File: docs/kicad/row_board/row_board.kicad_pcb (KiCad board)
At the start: 2 copper layers, 200 x 25 mm, 19 parts, among them J1 Conn_01x06, J2 Conn_01x06, SW1 SW1, SW2 SW1, SW3 SW1, SW4 SW1, SW5 SW1, U1 74HC595

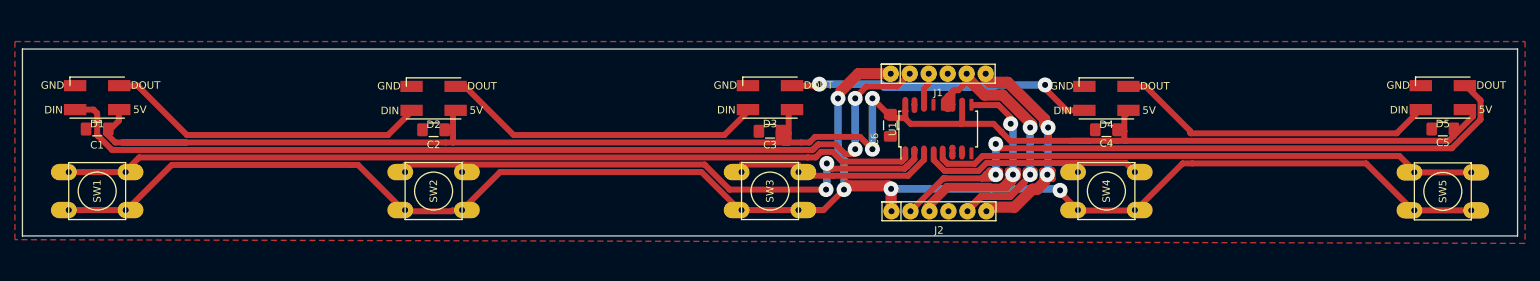
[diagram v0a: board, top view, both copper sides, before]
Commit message: new row board design (with chip at left end)
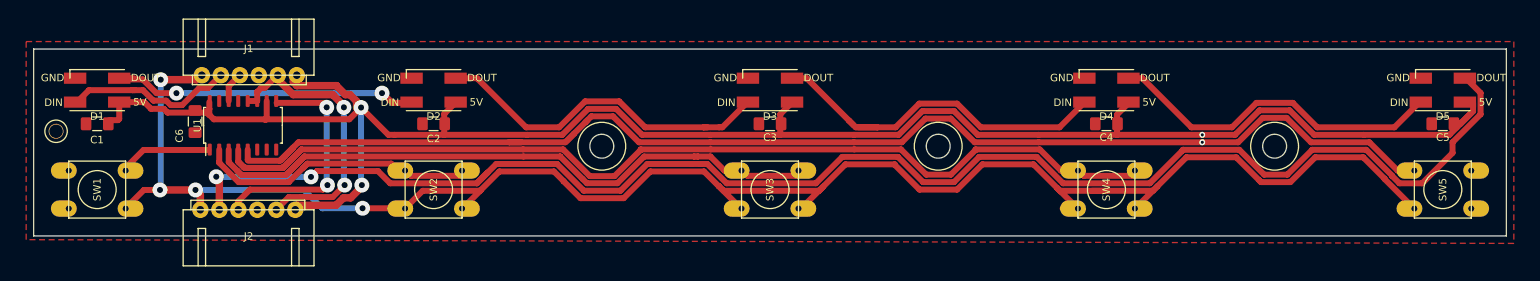
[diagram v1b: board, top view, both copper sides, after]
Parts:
- added REF**: myMountingHole_1.8mm, 0_my_footprints:myMountingHole_1.8mm, F.Cu at (54.5, 86.0)
- added REF**: myMountingHole_3.2mm_M3, 0_my_footprints:myMountingHole_3.2mm_M3, F.Cu at (217.5, 88.0)
- added REF**: myMountingHole_3.2mm_M3, 0_my_footprints:myMountingHole_3.2mm_M3, F.Cu at (172.5, 88.0)
- added REF**: myMountingHole_3.2mm_M3, 0_my_footprints:myMountingHole_3.2mm_M3, F.Cu at (127.5, 88.0)
- J1, J2: footprint 0_my_footprints:my6Pin-08mm -> 0_my_footprints:invRightAngleJSTx06
- moved J1 98.5 mm to (74.0, 78.5)
- moved C6 93.0 mm to (73.1, 84.7)
- moved U1 93.0 mm to (79.5, 85.2)
- moved J2 86.1 mm to (86.5, 96.5), turned to 180 degrees
- moved D2 1.10 mm to (105.0, 80.5)
- moved D4 1.10 mm to (195.0, 80.5)
- moved C3 1.00 mm to (150.0, 85.0)
- moved D1 1.00 mm to (60.0, 80.5)
- moved D3 1.00 mm to (150.0, 80.5)
- moved D5 1.00 mm to (240.0, 80.5)
- moved C2 0.80 mm to (105.0, 85.0)
- moved C4 0.80 mm to (195.0, 85.0)
- moved C1 0.70 mm to (60.0, 85.0)
- moved C5 0.70 mm to (240.0, 85.0)
- moved SW5 0.24 mm to (240.0, 93.8)
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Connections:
- J2 pad 1: BTN_SENSE -> +5V
- J2 pad 2: LED_DOUT -> BTN_CLK
- J2 pad 3: BTN_DOUT -> GND
- J2 pad 4: GND -> BTN_DOUT
- J2 pad 5: BTN_CLK -> LED_DOUT
- J2 pad 6: +5V -> BTN_SENSE
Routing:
- net Net-(SW4-Pad1): track 31.2 -> 142.3 mm
- net LED_DOUT: track 96.4 -> 204.8 mm
- net LED_DIN: track 126.1 -> 22.6 mm, vias 2 -> 0
- net Net-(SW1-Pad1): track 114.9 -> 12.4 mm
- net Net-(SW5-Pad1): track 73.7 -> 174.0 mm, vias 0 -> 1
- net Net-(SW3-Pad1): track 30.1 -> 87.9 mm
- net Net-(SW2-Pad1): track 79.5 -> 38.0 mm, vias 2 -> 0
- net +5V: track 273.3 -> 255.3 mm, vias 4 -> 3
- net BTN_DOUT: track 46.8 -> 31.9 mm
- net BTN_SENSE: track 230.1 -> 244.9 mm
- net Net-(D3-Pad2): track 40.3 -> 49.4 mm, vias 2 -> 0
- net BTN_CLK: track 43.7 -> 37.8 mm
- net Net-(D2-Pad2): track 43.3 -> 46.5 mm
- net Net-(D1-Pad2): track 43.4 -> 41.0 mm, vias 0 -> 2
- net Net-(D4-Pad2): track 43.5 -> 45.8 mm
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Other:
- board size 200 x 25 mm -> 197 x 25 mm
- board text removed: "NEEDS: Mounting Holes Ground Crossings -1 mm in height/width"

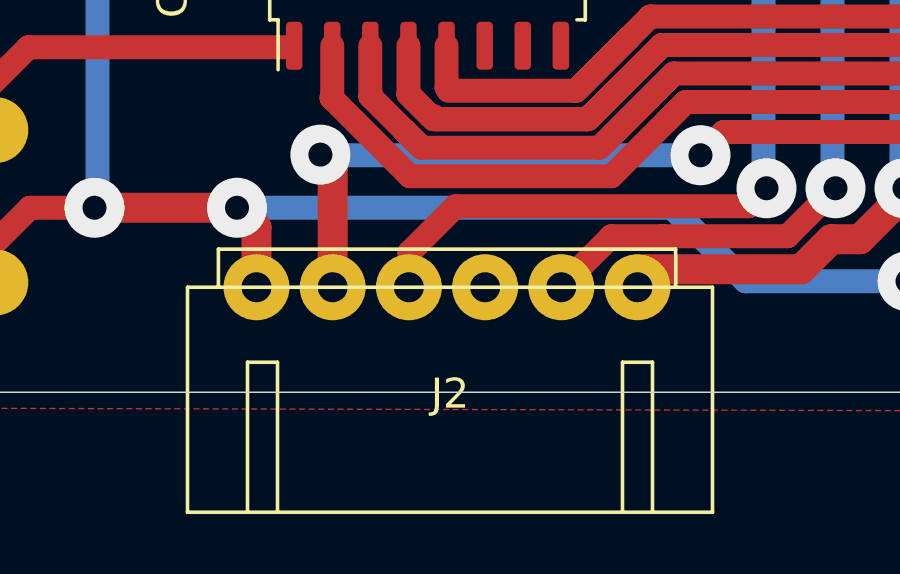
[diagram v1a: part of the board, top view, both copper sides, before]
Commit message: kicad changes to support actual Fusion 360 TE3 design efforts - created rotary board PCB
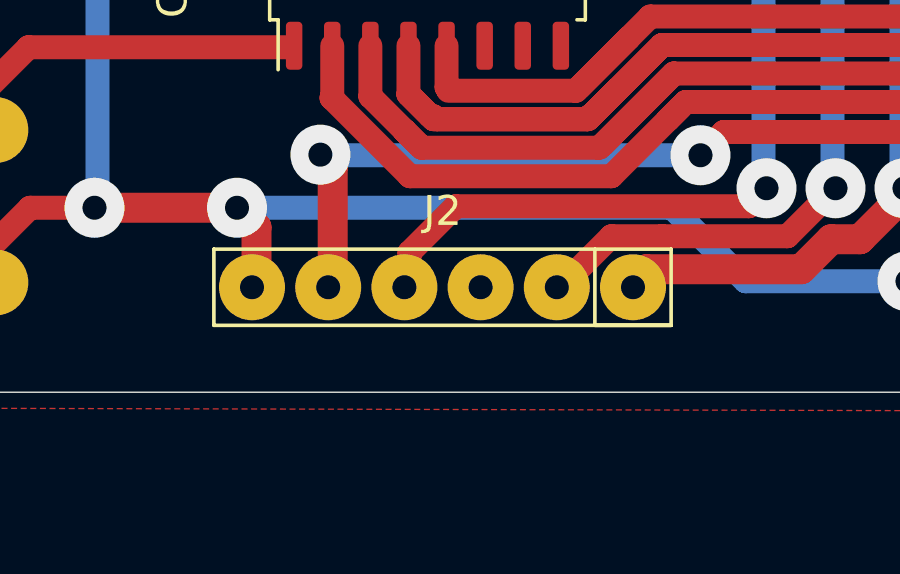
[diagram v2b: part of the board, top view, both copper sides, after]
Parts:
- J2: footprint 0_my_footprints:invRightAngleJSTx06 -> 0_my_footprints:my6Pin-08mm
- moved J2 6.50 mm to (80.0, 96.5)

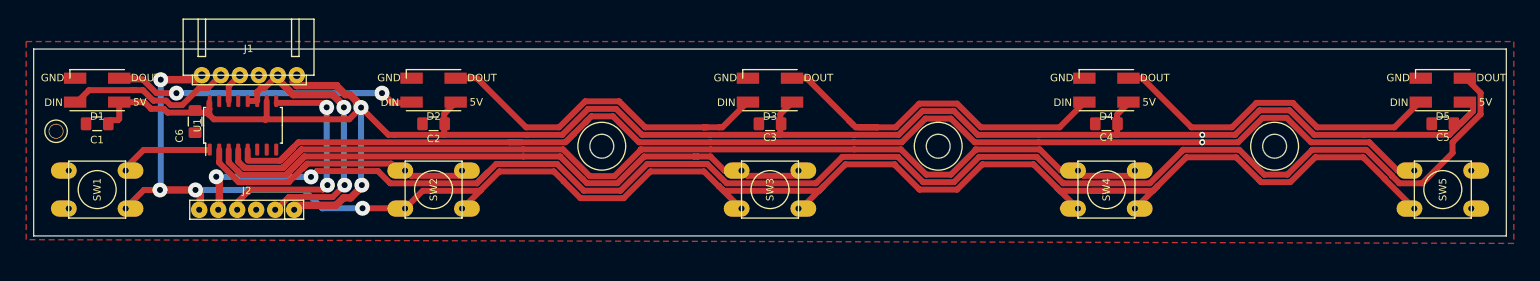
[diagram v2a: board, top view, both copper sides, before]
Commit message: cutting actual TE3 milled circuit boards
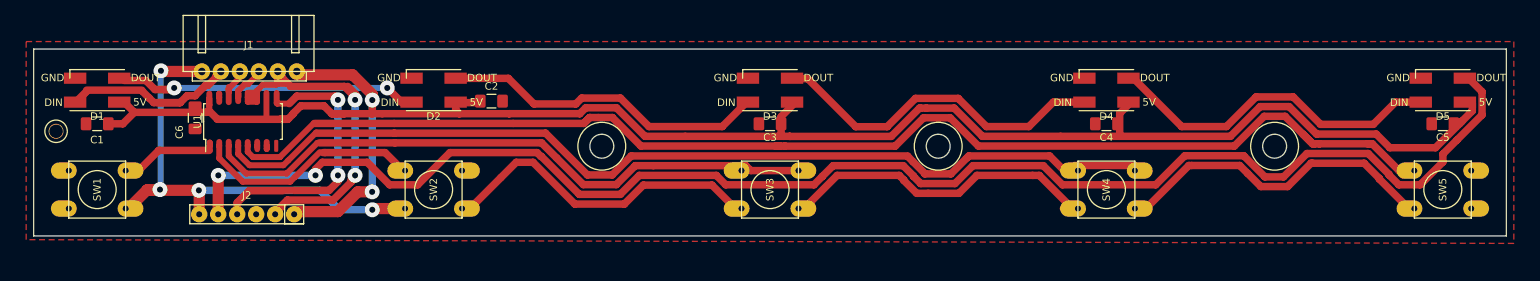
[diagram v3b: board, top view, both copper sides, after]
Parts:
- moved C2 8.31 mm to (112.7, 82.0), turned to 0 degrees
- moved J2 0.60 mm to (80.0, 97.1)
- moved C6 0.50 mm to (73.1, 84.2)
- moved J1 0.50 mm to (74.0, 78.0)
- moved U1 0.50 mm to (79.5, 84.7)
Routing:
- net BTN_SENSE: track 244.9 -> 202.1 mm
- net BTN_DOUT: track 31.9 -> 51.2 mm
- net BTN_CLK: track 37.8 -> 52.0 mm
- net Net-(SW4-Pad1): track 142.3 -> 131.3 mm
- net +5V: track 255.3 -> 265.2 mm, vias 3 -> 2
- net Net-(SW2-Pad1): track 38.0 -> 31.9 mm
- net GND: track 0.00 -> 5.98 mm
- net LED_DIN: track 22.6 -> 27.2 mm
- net Net-(D3-Pad2): track 49.4 -> 45.6 mm
- net Net-(D2-Pad2): track 46.5 -> 43.7 mm
- net Net-(SW3-Pad1): track 87.9 -> 86.0 mm
- net BTN_DIN: track 4.11 -> 5.94 mm
- net LED_DOUT: track 204.8 -> 203.2 mm
- net Net-(U1-Pad15): track 0.00 -> 1.11 mm
- net Net-(SW5-Pad1): track 174.0 -> 175.0 mm, vias 1 -> 0
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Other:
- net class Default: clearance 0.2 -> 0.3
- net class small removed
- rule trace_clearance: 0.2 -> 0.3
